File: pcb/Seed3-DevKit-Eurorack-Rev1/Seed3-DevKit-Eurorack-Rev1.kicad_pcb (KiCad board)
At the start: 2 copper layers, 141.9 x 111 mm, 137 parts, among them J7 USB4110GFA, Q1 MMBT3904, Q2 MMBT3904, SW1 TOGGLE_ON_OFF_ON_PIP2, SW2 TOGGLE_ON-ON_PIP3, SW3 PTH Mini Button, SW4 PTH Mini Button, U1 TL072, U11 H11L1, U12 CD4051B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

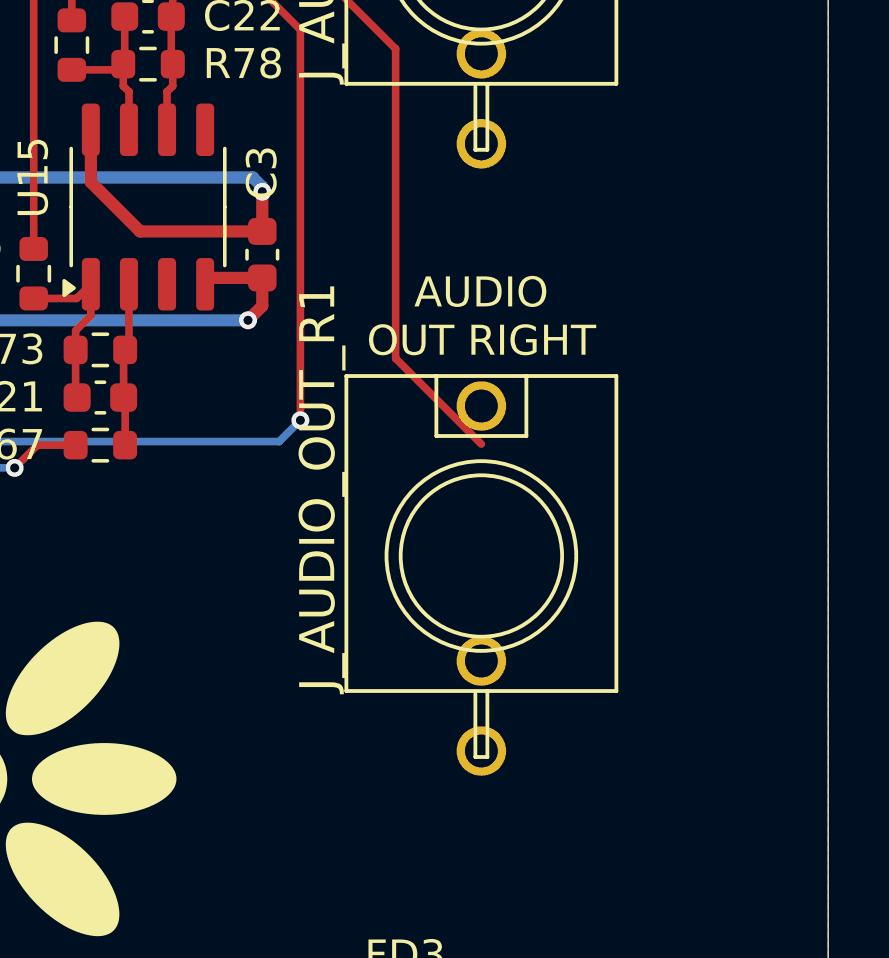
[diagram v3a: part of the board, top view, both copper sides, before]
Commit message: fixed misrouted pin, confirmed DRC
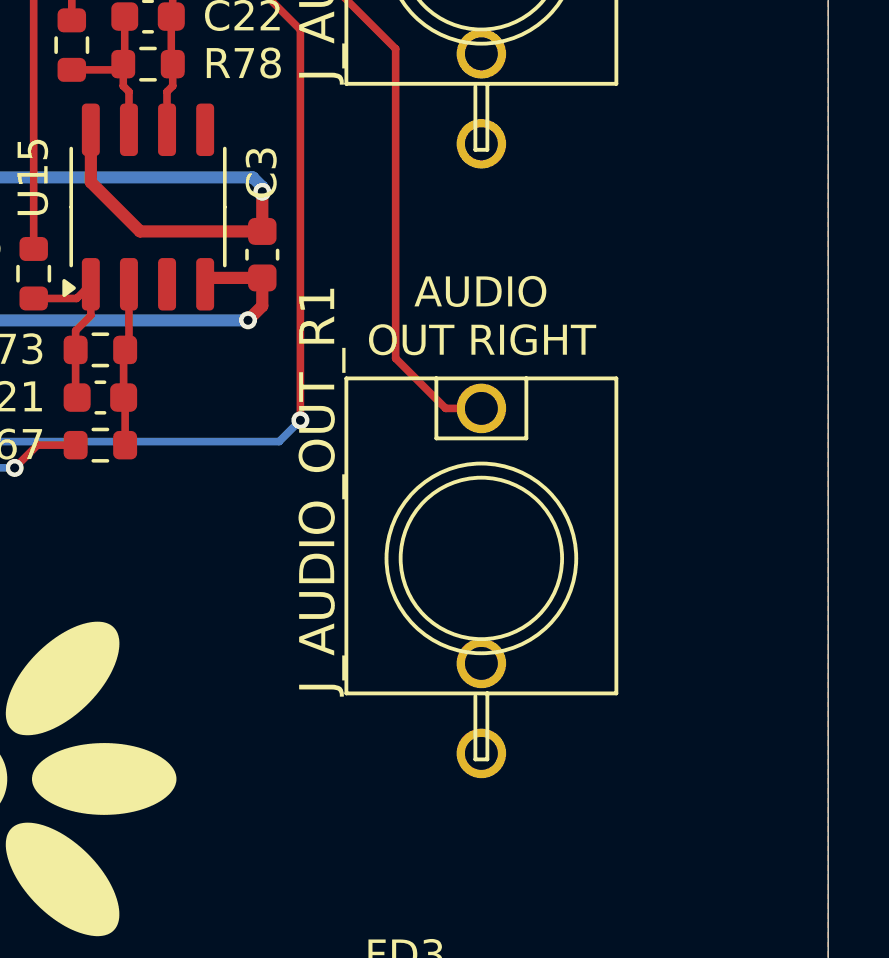
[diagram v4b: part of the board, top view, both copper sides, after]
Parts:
- moved J_AUDIO_OUT_R1 0.08 mm to (180.3, 134.6)
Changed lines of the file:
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@@
 	(footprint "Electrosmith-Interface:S_JACK"
 		(layer "F.Cu")
-		(at 180.34 134.54)
+		(at 180.34 134.62)
 		(property "Reference" "J_AUDIO_OUT_R1"
 			(at -4.7625 4.525 90)
@@
 			(polygon
 				(pts
-					(xy 179.07 135.81) (xy 181.61 135.81) (xy 181.61 133.27) (xy 179.07 133.27)
+					(xy 179.07 135.89) (xy 181.61 135.89) (xy 181.61 133.35) (xy 179.07 133.35)
 				)
 			)
@@
 	)
 	(segment
-		(start 180.34 130.81)
-		(end 177.4825 127.9525)
+		(start 177.4825 117.63375)
+		(end 172.72 112.87125)
 		(width 0.254)
 		(layer "F.Cu")
@@
 	)
 	(segment
-		(start 177.4825 117.63375)
-		(end 172.72 112.87125)
+		(start 166.6875 113.9825)
+		(end 166.6875 116.685)
 		(width 0.254)
 		(layer "F.Cu")
@@
 	)
 	(segment
-		(start 166.6875 113.9825)
-		(end 166.6875 116.685)
+		(start 180.34 129.62)
+		(end 179.15 129.62)
 		(width 0.254)
 		(layer "F.Cu")
@@
 		(width 0.254)
 		(layer "F.Cu")
+		(net 88)
+	)
+	(segment
+		(start 179.15 129.62)
+		(end 177.4825 127.9525)
+		(width 0.254)
+		(layer "F.Cu")
